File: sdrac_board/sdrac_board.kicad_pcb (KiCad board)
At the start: 4 copper layers, 81 x 51 mm, 131 parts, among them IC2 LMR16030PDDA, J1 SWD, J10 Pos_zero_sens, J11 SYNCHRONIZER, J2 Conn_01x02_Male, J3 Conn_01x02_Female, J4 STEPER_DRIVER_CONTROL, J5 STEPER_DRIVER_MOTOR_OUT, J6 USB_C_Receptacle_USB2.0, J7 Conn_01x02, J8 Conn_01x02, J9 Mag_enc, SW1 BOOT0, SW2 NRST, SW3 USR_BTN, SW4 SW_DIP_x01, U1 FM24CL16B, U10 USBLC6-2SC6, U11 MCP9700AT-ETT, U2 STM32F412RGT6, U3 SN65HVD232, U4 CAN, U5 CAN, U6 AZ1117-3.3, U7 SN74LV1T34DBV, U8 SN74LV1T34DBV, U9 SN74LV1T34DBV, Y1 16MHz

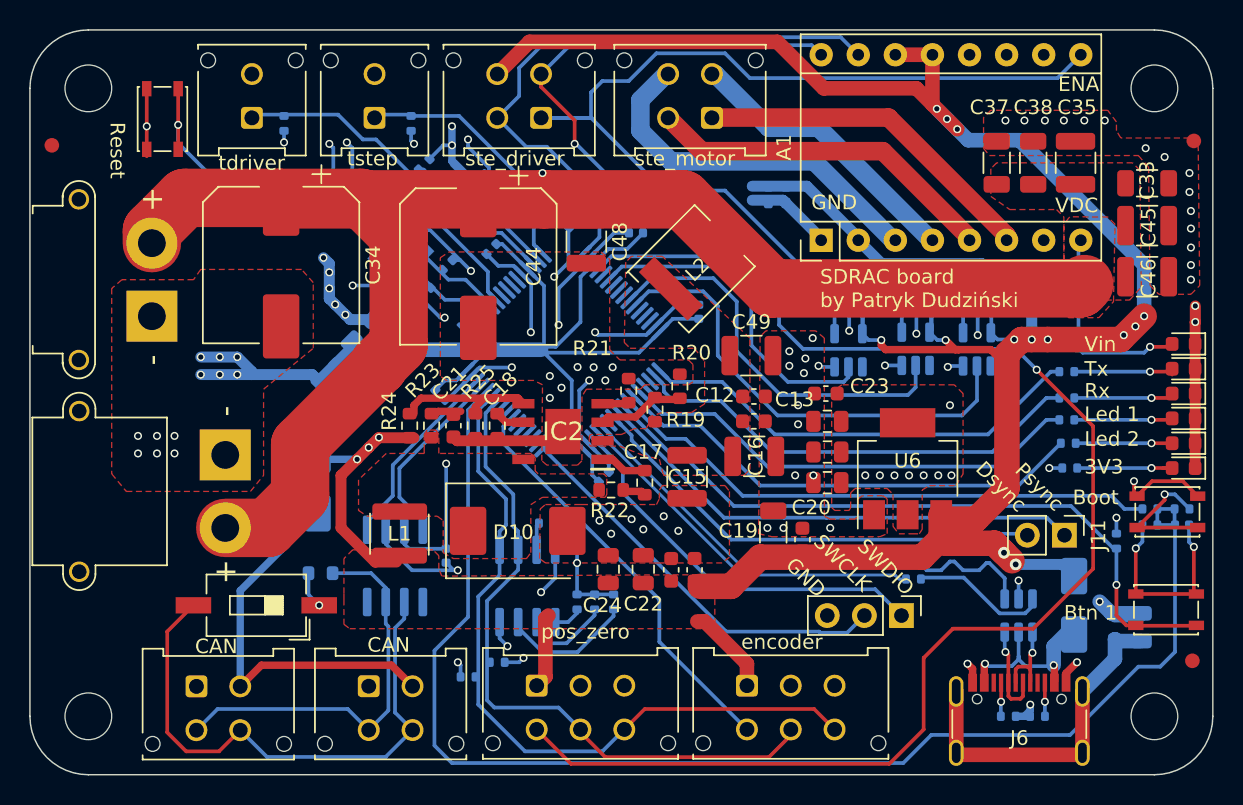
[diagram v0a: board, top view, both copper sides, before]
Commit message: fixed caps and added nreset
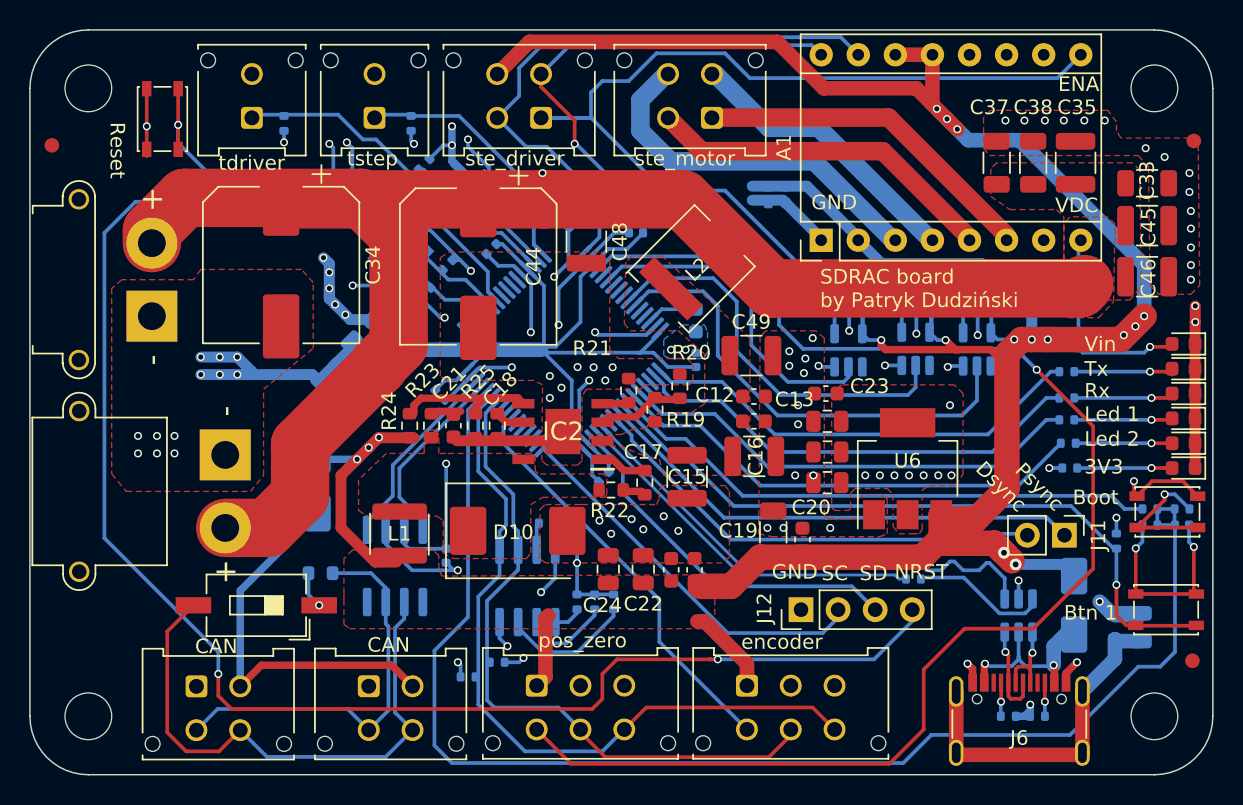
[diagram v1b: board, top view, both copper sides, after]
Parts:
- removed J1: SWD, Connector_PinHeader_2.54mm:PinHeader_1x03_P2.54mm_Vertical
- added C14: 2.2u, Capacitor_SMD:C_0603_1608Metric, B.Cu at (146.5, 82.5)
- added J12: SWD, Connector_PinHeader_2.54mm:PinHeader_1x04_P2.54mm_Vertical, F.Cu at (153.7, 102.3)
- moved C5 3.31 mm to (146.5, 85.2)
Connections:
- U2 pad 30: unconnected-(U2-VCAP_1-Pad30) -> Net-(U2-VCAP_1)
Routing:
- net /MCU/NRST: track 32.6 -> 129.8 mm, vias 1 -> 3
- net GND: track 162.0 -> 158.4 mm, vias 83 -> 85
- net Net-(U2-VCAP_1): track 0.00 -> 3.48 mm
- net /MCU/SWDIO: track 27.1 -> 25.7 mm
- net /MCU/3V3_MCU: track 72.8 -> 74.2 mm
- net /MCU/SWCLK: track 27.7 -> 26.4 mm
- added copper zone on In1.Cu, net +3V3
- added copper zone on B.Cu, net GND
- added copper zone on In2.Cu, net GND
- removed copper zone on In2.Cu, net +3V3
- removed copper zone on In1.Cu, net GND
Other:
- board text added: "NRST"
- board text added: "SC"
- board text added: "SD"
- board text removed: "SWCLK"
- board text removed: "SWDIO"

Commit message: addded 6pin conenctor
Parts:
- added J1: INOUT, Connector_PinHeader_2.54mm:PinHeader_1x06_P2.54mm_Vertical, F.Cu at (179.6, 92.8)
- moved R18 21.3 mm to (177.6, 72.0)
- moved C33 18.8 mm to (158.9, 69.7), turned to 90 degrees
- moved D8 17.3 mm to (179.9, 75.3)
- moved R17 14.0 mm to (177.6, 70.8), turned to 0 degrees
- moved D7 10.5 mm to (179.9, 73.6)
- moved C46 8.69 mm to (174.0, 71.5), turned to 90 degrees
- moved C45 8.15 mm to (170.6, 71.5), turned to 90 degrees
- moved C37 5.95 mm to (161.5, 69.7)
- moved C38 5.85 mm to (164.1, 69.7)
- moved C35 5.66 mm to (167.2, 69.7)
- moved D3 5.10 mm to (174.9, 90.2)
- moved D4 5.10 mm to (174.9, 91.9)
- moved D5 5.10 mm to (174.9, 88.5)
- moved D6 5.10 mm to (174.9, 86.8)
- moved R8 2.82 mm to (169.5, 92.2)
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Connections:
- U2 pad 21: unconnected-(U2-PA5-Pad21) -> /MCU/C_A1
- U2 pad 23: unconnected-(U2-PA7-Pad23) -> /MCU/C_A2
- U2 pad 24: unconnected-(U2-PC4-Pad24) -> /MCU/C_D1
- U2 pad 25: unconnected-(U2-PC5-Pad25) -> /MCU/C_D2
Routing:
- net /MCU/C_D2: track 0.00 -> 44.3 mm, vias 0 -> 1
- net /MCU/C_D1: track 0.00 -> 43.1 mm, vias 0 -> 1
- net /MCU/C_A1: track 0.00 -> 42.9 mm, vias 0 -> 1
- net /MCU/C_A2: track 0.00 -> 42.3 mm, vias 0 -> 1
- net +5V: track 202.9 -> 214.2 mm, vias 16 -> 14
- net +3V3: track 40.8 -> 46.7 mm
- net /MCU/USR_LED1: track 32.2 -> 29.2 mm
- net /MCU/USR_LED2: track 32.9 -> 30.0 mm
- net /CAN/RXD_LED: track 31.6 -> 28.7 mm
- net /CAN/TXD_LED: track 30.9 -> 28.1 mm
- net Net-(D7-A): track 6.74 -> 4.10 mm
- net Net-(D8-A): track 6.72 -> 4.10 mm
- net Net-(D5-A): track 6.70 -> 4.37 mm
- net Net-(D6-A): track 6.79 -> 4.51 mm
- net Net-(D3-A): track 6.70 -> 4.47 mm
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
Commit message: updated stuf
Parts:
- moved D3 2.42 mm to (172.5, 90.5)
- moved D4 2.42 mm to (172.5, 92.2)
- moved D5 2.42 mm to (172.5, 88.8)
- moved D6 2.42 mm to (172.5, 87.1)
- moved R8 1.20 mm to (168.3, 92.2)
- moved R12 1.10 mm to (168.3, 88.9)
- moved R13 1.10 mm to (168.3, 87.2)
- moved R3 1.10 mm to (168.3, 90.5)
- moved SW1 0.10 mm to (178.7, 97.3)
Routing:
- net /MCU/Poz_zero_sens: track 98.4 -> 100.9 mm
- net Net-(D3-A): track 4.47 -> 2.90 mm
- net Net-(D6-A): track 4.51 -> 2.94 mm
- net Net-(D4-A): track 4.37 -> 2.90 mm
- net Net-(D5-A): track 4.37 -> 2.94 mm
- net /CAN/TXD_LED: track 28.1 -> 26.8 mm
- net /MCU/USR_LED2: track 30.0 -> 28.7 mm
- net /CAN/RXD_LED: track 28.7 -> 27.6 mm
- net /MCU/USR_LED1: track 29.2 -> 28.1 mm
- net GND: track 157.2 -> 158.2 mm, vias 92 -> 93
- net +5V: track 214.2 -> 214.5 mm, vias 14 -> 16
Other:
- board text added: "Btn1"
- board text added: "CA1"
- board text added: "CA2"
- board text added: "CD1"
- board text added: "CD2"
- board text added: "DS"
- board text added: "Led1"
- board text added: "Led2"
- board text added: "PS"
- board text removed: "Btn 1"
- board text removed: "Dsync"
- board text removed: "Led 1"
- board text removed: "Led 2"
- board text removed: "Psync"

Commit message: stuff
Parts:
- J1: footprint Connector_PinHeader_2.54mm:PinHeader_1x06_P2.54mm_Vertical -> Connector_JST:JST_XH_B6B-XH-A_1x06_P2.50mm_Vertical
- J11: footprint Connector_PinHeader_2.54mm:PinHeader_1x02_P2.54mm_Vertical -> Connector_JST:JST_XH_B2B-XH-A_1x02_P2.50mm_Vertical
- moved D3 1.70 mm to (170.8, 90.5)
- moved D4 1.70 mm to (170.8, 92.2)
- moved D5 1.70 mm to (170.8, 88.8)
- moved D6 1.70 mm to (170.8, 87.1)
- moved J1 1.60 mm to (178.1, 92.2), turned to 90 degrees
- moved R12 0.80 mm to (167.5, 88.9)
- moved R13 0.80 mm to (167.5, 87.2)
- moved R3 0.80 mm to (167.5, 90.5)
- moved R8 0.80 mm to (167.5, 92.2)
- moved J11 0.08 mm to (171.8, 97.1), turned to 180 degrees
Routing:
- net +3V3: track 46.7 -> 40.7 mm
- net +5V: track 214.5 -> 211.0 mm
- net GND: track 158.2 -> 156.2 mm, vias 93 -> 94
- net /MCU/C_D1: track 42.9 -> 41.1 mm
- net /MCU/C_A2: track 42.4 -> 40.7 mm
- net /MCU/C_A1: track 43.0 -> 41.3 mm
- net /MCU/C_D2: track 44.4 -> 42.8 mm
- net Net-(D6-A): track 2.94 -> 1.90 mm
- net Net-(D5-A): track 2.94 -> 2.04 mm
- net Net-(D4-A): track 2.90 -> 2.00 mm
- net Net-(D3-A): track 2.90 -> 2.00 mm
- net /MCU/USR_LED2: track 28.7 -> 27.9 mm
- net /CAN/RXD_LED: track 27.6 -> 26.8 mm
- net /MCU/USR_LED1: track 28.1 -> 27.3 mm
- net /CAN/TXD_LED: track 26.8 -> 26.1 mm

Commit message: made critical changes
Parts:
- moved R13 0.70 mm to (167.5, 87.9)
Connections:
- net /MCU/C_D1 renamed /MCU/C_RX
- J1 pad 2: /MCU/C_D2 -> /MCU/C_TX
- U2 pad 25: /MCU/C_D2 -> unconnected-(U2-PC5-Pad25)
- U2 pad 29: unconnected-(U2-PB10-Pad29) -> /MCU/C_TX
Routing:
- net /MCU/C_TX: track 0.00 -> 42.9 mm
- net /MCU/C_D2: track 42.8 -> 0.00 mm, vias 1 -> 0
- net /MCU/BOOT0: track 93.4 -> 91.0 mm
- net +5V: track 211.0 -> 212.7 mm
- net VCC: track 112.7 -> 111.5 mm
- net /MCU/MCU_STEPER_ENABLE: track 31.5 -> 30.4 mm
- net /MCU/Poz_zero_sens: track 100.9 -> 100.4 mm
- net /MCU/MCU_STEPER_DIRECTION: track 26.1 -> 26.6 mm
- net GND: vias 94 -> 93
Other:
- board text added: "CRX"
- board text added: "CTX"
- board text removed: "CD1"
- board text removed: "CD2"

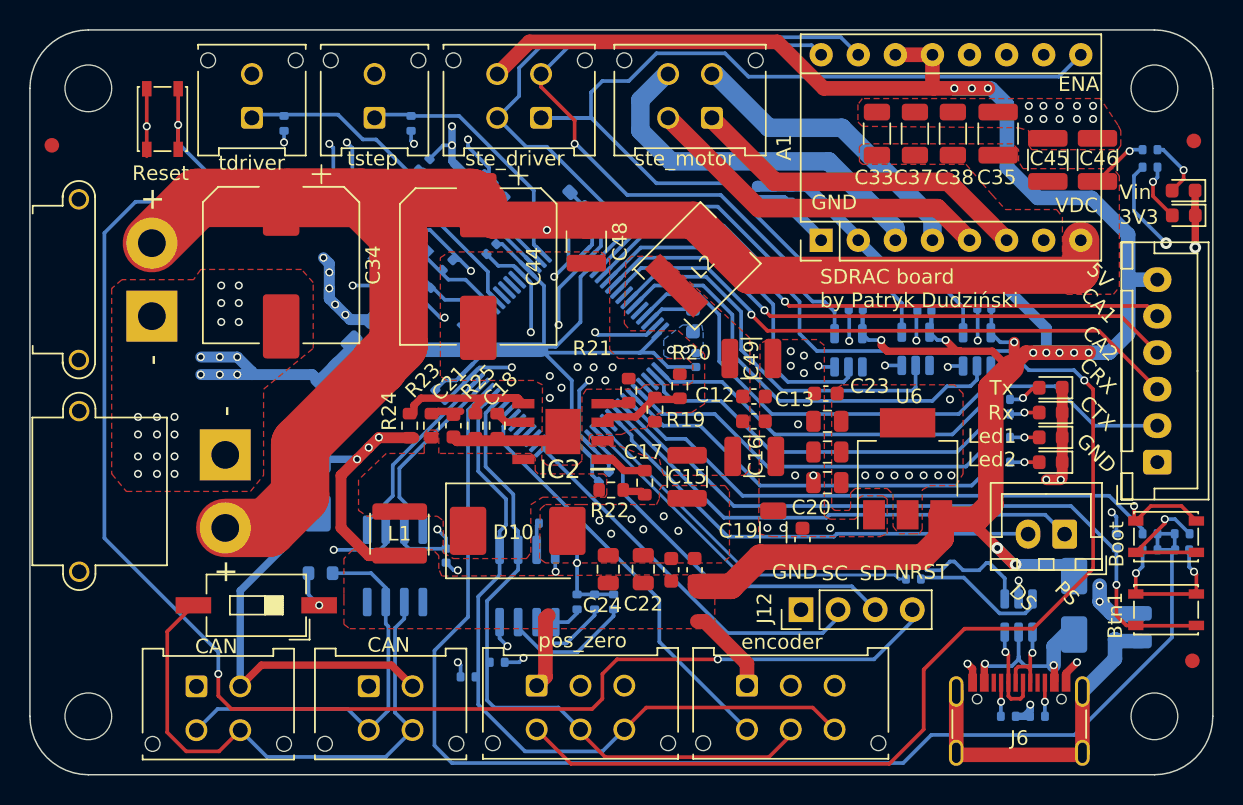
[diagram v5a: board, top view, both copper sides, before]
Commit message: added second I2C communscation lane for synchronization and added wyas to change mcirosteping with resistors
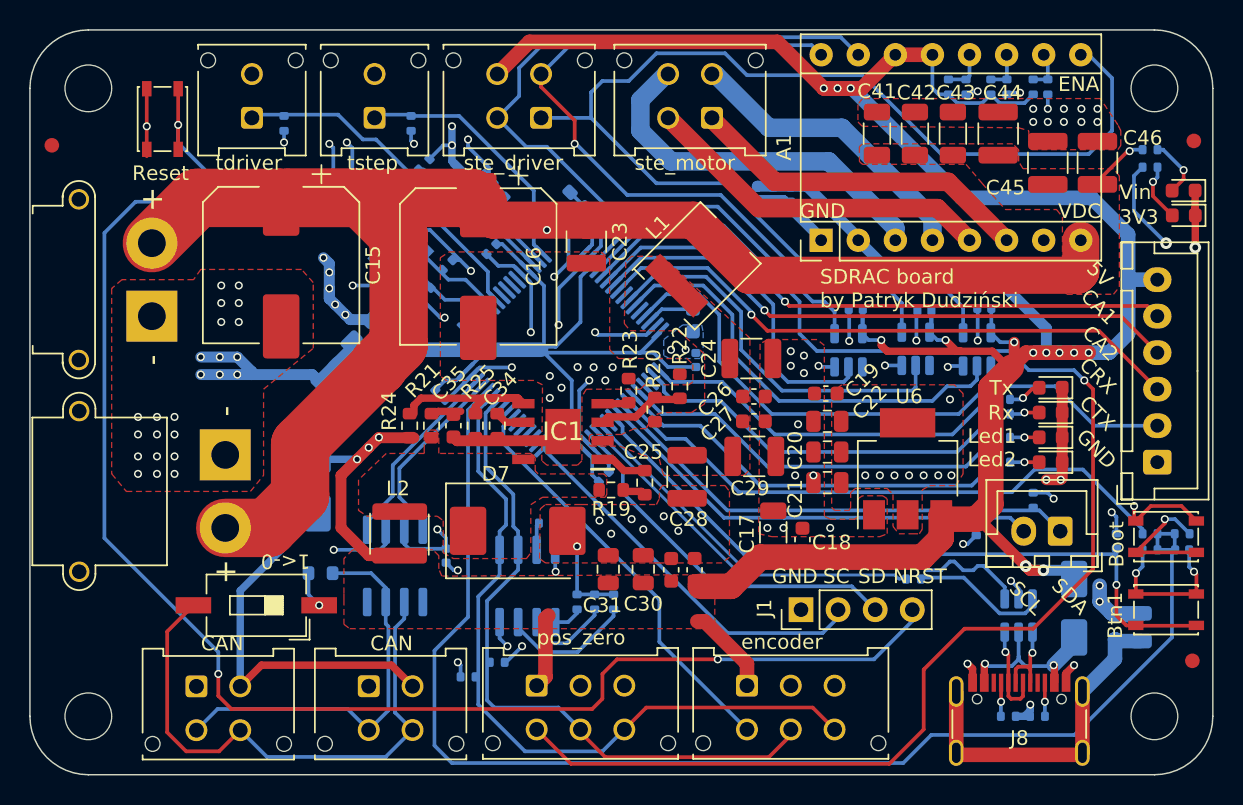
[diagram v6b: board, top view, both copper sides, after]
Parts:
- added R30: 10k, Resistor_SMD:R_0402_1005Metric, B.Cu at (170.6, 66.5)
- added R31: 10k, Resistor_SMD:R_0402_1005Metric, B.Cu at (169.6, 66.5)
- added R32: 10k, Resistor_SMD:R_0402_1005Metric, B.Cu at (167.8, 66.5)
- added R33: 10k, Resistor_SMD:R_0402_1005Metric, B.Cu at (166.7, 66.5)
- added R34: 10k, Resistor_SMD:R_0402_1005Metric, B.Cu at (165.0, 66.5)
- added R35: 10k, Resistor_SMD:R_0402_1005Metric, B.Cu at (163.8, 66.5)
- added R7: 4k7, Resistor_SMD:R_0402_1005Metric, B.Cu at (169.6, 94.8)
- added R8: 4k7, Resistor_SMD:R_0402_1005Metric, B.Cu at (165.7, 96.7)
- moved J2 0.36 mm to (171.4, 96.9)
- moved C45 0.20 mm to (170.6, 71.7)
- moved C46 0.20 mm to (174.0, 71.7)
- moved D2 0.20 mm to (172.4, 102.2)
- renumbered C36 to C1, C47 to C10, C2 to C11, C3 to C12, C14 to C13, C11 to C14, C34 to C15, C44 to C16, C19 to C17, C20 to C18, C23 to C19, C4 to C2, C25 to C20, C27 to C21, C29 to C22, C48 to C23, C49 to C24, C17 to C25, C12 to C26, C13 to C27, C15 to C28, C16 to C29, C5 to C3, C22 to C30, C24 to C31, C26 to C32, C28 to C33, C18 to C34, C21 to C35, C40 to C36, C41 to C37, C30 to C38, C31 to C39, C6 to C4, C32 to C40, C33 to C41, C37 to C42, C38 to C43, C35 to C44, C39 to C47, C42 to C48, C43 to C49, C7 to C5, C8 to C6, C9 to C7, C10 to C8, C1 to C9, D2 to D1, D1 to D2, D10 to D7, D7 to D8, D8 to D9, IC2 to IC1, J12 to J1, J9 to J10, J10 to J11, J8 to J12, J11 to J2, J1 to J3, J2 to J4, J3 to J5, J4 to J6, J5 to J7, J6 to J8, J7 to J9, L2 to L1, L1 to L2, R34 to R1, R2 to R10, R5 to R11, R7 to R12, R11 to R13, R3 to R14, R8 to R15, R14 to R16, R12 to R17, R13 to R18, R22 to R19, R10 to R2, R19 to R20, R23 to R21, R20 to R22, R21 to R23, R15 to R26, R17 to R27, R18 to R28, R16 to R29, R35 to R3, R27 to R36, R28 to R37, R29 to R38, R30 to R39, R26 to R40, R31 to R41, R33 to R42, R32 to R43, R6 to R5, R9 to R6, R1 to R9, U2 to U1, U1 to U2, U8 to U7, U9 to U8, U7 to U9
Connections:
- A1 pad 10: unconnected-(A1-MS1-Pad10) -> Net-(A1-MS1)
- A1 pad 11: unconnected-(A1-MS2-Pad11) -> Net-(A1-MS2)
- A1 pad 12: unconnected-(A1-MS3-Pad12) -> Net-(A1-MS3)
- J2 pad 1: /MCU/PUL_SYNC -> /MCU/SYNC_I2C_SDA
- J2 pad 2: /MCU/DIR_SYNC -> /MCU/SYNC_I2C_SCL
- U1 pad 40: /MCU/USR_BTN -> /MCU/SYNC_I2C_SDA
- U1 pad 41: /MCU/PUL_SYNC -> /MCU/SYNC_I2C_SCL
- U1 pad 42: /MCU/DIR_SYNC -> /MCU/USR_BTN
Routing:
- net /MCU/PUL_SYNC: track 34.3 -> 0.00 mm
- net /MCU/SYNC_I2C_SDA: track 0.00 -> 33.5 mm
- net /MCU/DIR_SYNC: track 32.0 -> 0.00 mm
- net /MCU/SYNC_I2C_SCL: track 0.00 -> 31.1 mm
- net +5V: track 212.7 -> 222.7 mm
- net /SteperMotor/STEPER_ENABLE: track 77.2 -> 84.5 mm
- net Net-(A1-MS3): track 0.00 -> 2.99 mm
- net +3V3: track 40.7 -> 43.6 mm, vias 24 -> 26
- net Net-(A1-MS1): track 0.00 -> 2.81 mm
- net Net-(A1-MS2): track 0.00 -> 2.80 mm
- net GND: track 156.2 -> 158.8 mm, vias 93 -> 95
- net /MCU/BOOT_EN: track 39.1 -> 40.4 mm
- net /MCU/USR_BTN: track 48.1 -> 49.2 mm
- net /USB/V_BUS: track 13.2 -> 12.3 mm
- net Net-(R38-Pad1): track 8.46 -> 7.94 mm
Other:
- board text removed: "DS"
- board text removed: "PS"

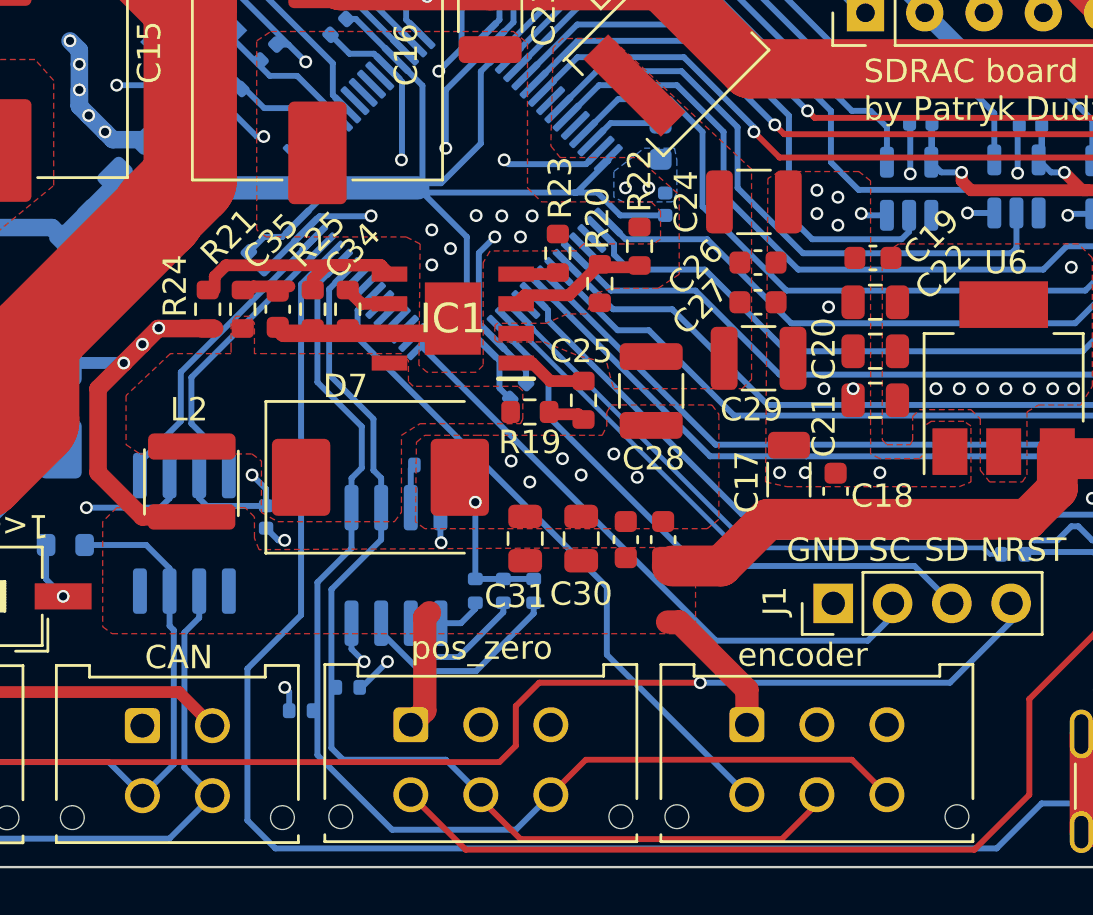
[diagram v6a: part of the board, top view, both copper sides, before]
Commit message: added hardware address selector
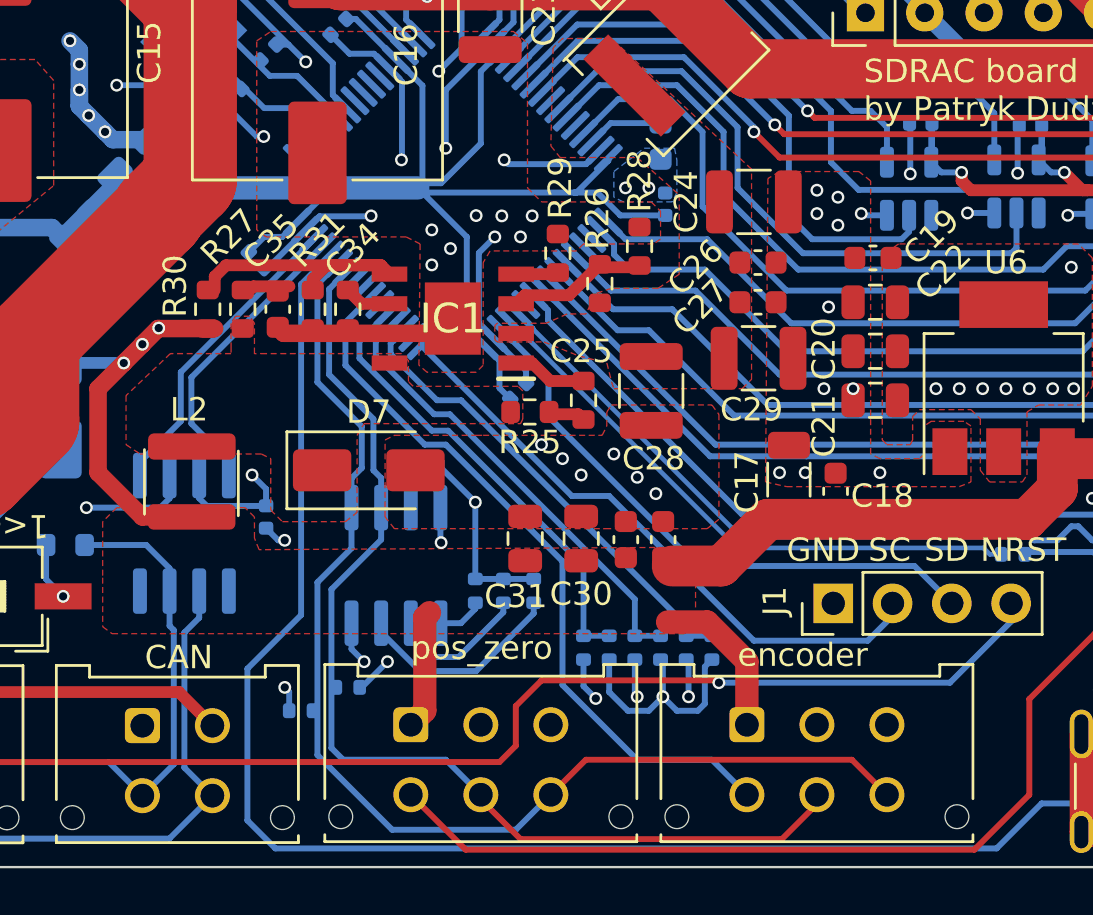
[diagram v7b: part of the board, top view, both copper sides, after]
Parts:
- added R13: 10k, Resistor_SMD:R_0402_1005Metric, B.Cu at (144.1, 104.2)
- added R14: 10k, Resistor_SMD:R_0402_1005Metric, B.Cu at (146.3, 104.2)
- added R15: 10k, Resistor_SMD:R_0402_1005Metric, B.Cu at (148.5, 104.2)
- added R19: 10k, Resistor_SMD:R_0402_1005Metric, B.Cu at (143.0, 104.2)
- added R20: 10k, Resistor_SMD:R_0402_1005Metric, B.Cu at (145.2, 104.2)
- added R21: 10k, Resistor_SMD:R_0402_1005Metric, B.Cu at (147.4, 104.2)
- D7: footprint Diode_SMD:D_SMC -> Diode_SMD:D_SMA
- moved D7 0.58 mm to (133.8, 96.6)
- renumbered R13 to R16, R14 to R17, R15 to R18, R16 to R22, R17 to R23, R18 to R24, R19 to R25, R20 to R26, R21 to R27, R22 to R28, R23 to R29, R24 to R30, R25 to R31, R26 to R32, R27 to R33, R28 to R34, R29 to R35, R30 to R36, R31 to R37, R32 to R38, R33 to R39, R34 to R40, R35 to R41, R36 to R42, R37 to R43, R38 to R44, R39 to R45, R40 to R46, R41 to R47, R42 to R48, R43 to R49
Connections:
- U1 pad 51: unconnected-(U1-PC10-Pad51) -> /MCU/CHIP_ID_0
- U1 pad 52: unconnected-(U1-PC11-Pad52) -> /MCU/CHIP_ID_1
- U1 pad 53: unconnected-(U1-PC12-Pad53) -> /MCU/CHIP_ID_2
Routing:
- net /MCU/CHIP_ID_0: track 0.00 -> 20.3 mm
- net /MCU/CHIP_ID_1: track 0.00 -> 19.9 mm
- net /MCU/CHIP_ID_2: track 0.00 -> 19.9 mm
- net +3V3: track 43.6 -> 53.7 mm, vias 26 -> 27
- net GND: track 158.8 -> 164.0 mm, vias 95 -> 98
- net /MCU/Mag_enc_analog: track 28.7 -> 31.5 mm
- net +5V: track 222.7 -> 223.4 mm
